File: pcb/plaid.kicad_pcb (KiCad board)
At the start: 2 copper layers, 228 x 98 mm, 127 parts, among them J2 AVR_ISP_6, SW1 SW_Push, SW10 SW_Push, SW11 SW_Push, SW12 SW_Push, SW13 SW_Push, SW14 SW_Push, SW15 SW_Push, SW16 SW_Push, SW17 SW_Push, SW18 SW_Push, SW19 SW_Push, SW2 SW_Push, SW20 SW_Push, SW21 SW_Push, SW22 SW_Push, SW23 SW_Push, SW24 SW_Push, SW25 SW_Push, SW26 SW_Push, SW27 SW_Push, SW28 SW_Push, SW29 SW_Push, SW3 SW_Push, SW30 SW_Push, SW31 SW_Push, SW32 SW_Push, SW33 SW_Push, SW34 SW_Push, SW35 SW_Push, SW36 SW_Push, SW37 SW_Push, SW38 SW_Push, SW39 SW_Push, SW4 SW_Push, SW40 SW_Push, SW41 SW_Push, SW42 SW_Push, SW43 SW_Push, SW44 SW_Push, SW45 SW_Push, SW46 SW_Push, SW47 SW_Push, SW48 SW_Push, SW49 SW_Push, SW5 SW_Push, SW50 RESET, SW51 BOOT, SW6 SW_Push, SW7 SW_Push, SW8 SW_Push, SW9 SW_Push, U1 ATMEGA328-PU, Y1 16MHz

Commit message: RGB LED setup
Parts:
- added 100n: 100n, Capacitor_THT:C_Disc_D4.3mm_W1.9mm_P5.00mm, F.Cu at (269.5, 59.3)
- added D49: SK6812, LED_SMD:LED_SK6812_PLCC4_5.0x5.0mm_P3.2mm, F.Cu at (259.5, 54.1)
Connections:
- net /i2c_SCL renamed Net-(U1-Pad28)
- U1 pad 27: /i2c_SDA -> /RGB_LED
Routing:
- net /RGB_LED: track 0.00 -> 33.5 mm, vias 0 -> 1
- net +5V: track 91.2 -> 123.2 mm
- net /i2c_SDA: track 2.69 -> 0.00 mm

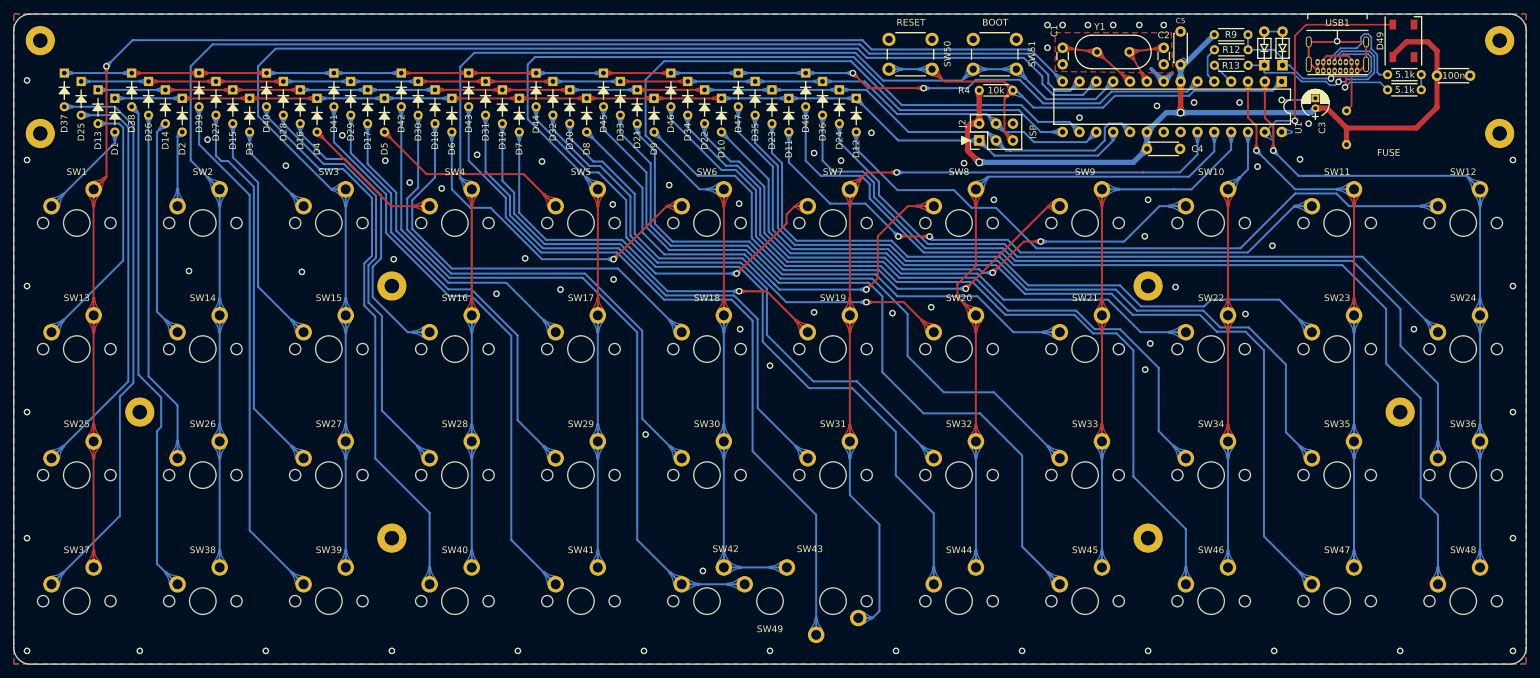
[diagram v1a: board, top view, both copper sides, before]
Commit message: Add usb-c, rgb led
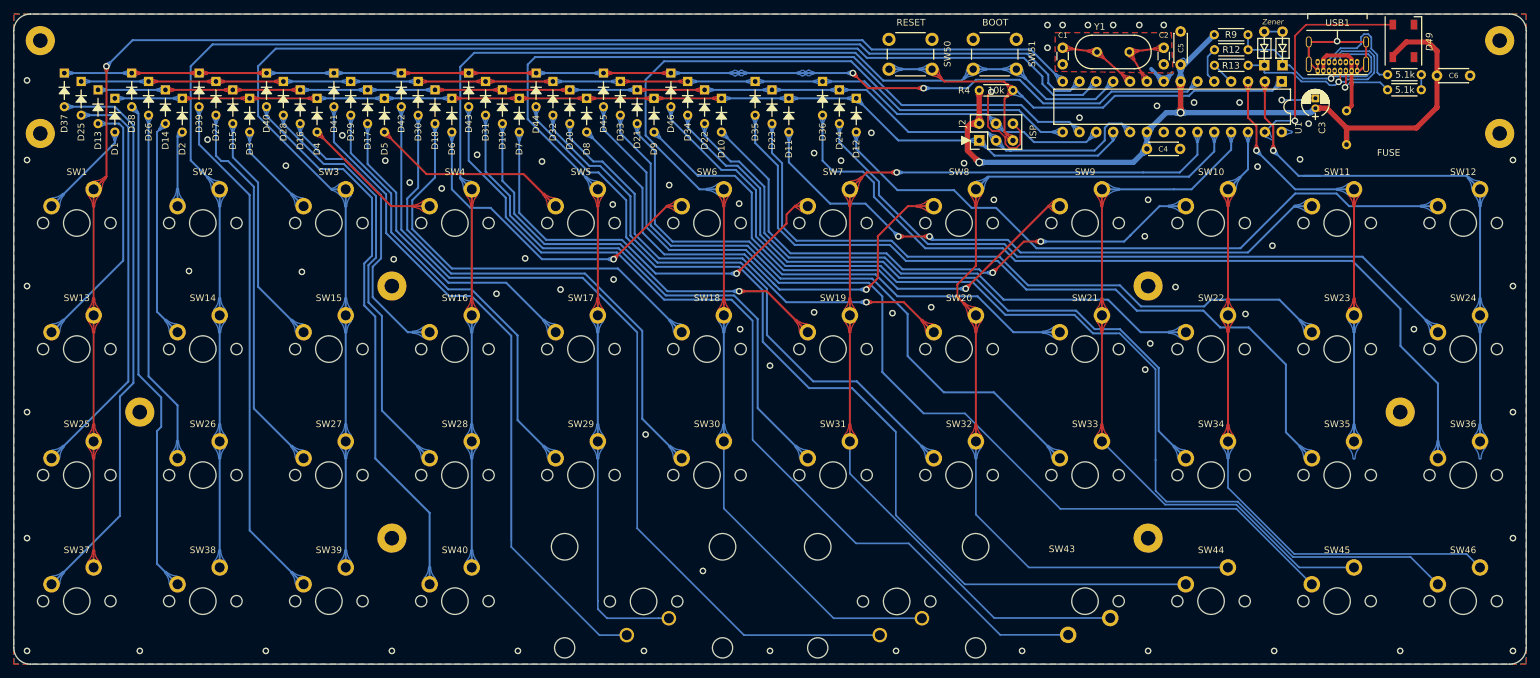
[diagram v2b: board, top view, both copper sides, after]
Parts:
- removed D47, D48: 1N4148, dm9_rc:D_DO-35_SOD27_P5.08mm_Horizontal
- removed SW47, SW48: SW_Push, SMKJP:SW_Cherry_MX1A_1.00u_PCB
- removed SW49: SW_Push, SMKJP:SW_Cherry_MX1A_2.0U_PCB_universal_center
- SW41, SW42: footprint SMKJP:SW_Cherry_MX1A_1.00u_PCB -> cftkb:SW_Cherry_MX1A_2.00u_PCBNOSCREEN
- moved SW43 38.0 mm to (211.5, 138.5)
- moved SW44 38.0 mm to (230.5, 138.5)
- moved SW45 38.0 mm to (249.5, 138.5)
- moved SW46 38.0 mm to (268.5, 138.5)
- moved SW42 26.6 mm to (180.6, 143.6), turned to 180 degrees
- moved SW41 8.60 mm to (142.4, 143.6), turned to 180 degrees
- renumbered 100n to C6
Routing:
- net Net-(D48-Pad2): track 150.9 -> 0.00 mm
- net Net-(D47-Pad2): track 140.5 -> 0.00 mm
- net Net-(D44-Pad2): track 108.8 -> 143.6 mm
- net /COL7: track 100.6 -> 133.9 mm
- net Net-(D46-Pad2): track 128.7 -> 161.4 mm
- net /COL9: track 66.9 -> 97.8 mm
- net Net-(D45-Pad2): track 120.2 -> 150.1 mm
- net /COL8: track 81.6 -> 108.5 mm
- net Net-(D43-Pad2): track 114.0 -> 140.3 mm
- net Net-(D42-Pad2): track 110.8 -> 133.3 mm
- net /COL6: track 127.0 -> 149.1 mm
- net /COL11: track 103.9 -> 84.9 mm
- net /COL10: track 85.1 -> 66.1 mm
- net /COL5: track 158.5 -> 176.8 mm
- net /COL4: track 168.5 -> 186.1 mm
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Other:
- net class VCC added: clearance 0.2, trace_width 0.6, via_dia 1, via_drill 0.6
- board text added: "D1"
- board text added: "D10"
- board text added: "D11"
- board text added: "D12"
- board text added: "D13"
- board text added: "D14"
- board text added: "D15"
- board text added: "D16"
- board text added: "D17"
- board text added: "D18"
- board text added: "D19"
- board text added: "D2"
- board text added: "D20"
- board text added: "D21"
- board text added: "D22"
- board text added: "D23"
- board text added: "D24"
- board text added: "D25"
- board text added: "D26"
- board text added: "D27"
- board text added: "D28"
- board text added: "D29"
- board text added: "D3"
- board text added: "D30"
- board text added: "D31"
- board text added: "D32"
- board text added: "D33"
- board text added: "D34"
- board text added: "D35"
- board text added: "D36"
- board text added: "D37"
- board text added: "D38"
- board text added: "D39"
- board text added: "D4"
- board text added: "D40"
- board text added: "D41"
- board text added: "D42"
- board text added: "D43"
- board text added: "D44"
- board text added: "D45"
- board text added: "D46"
- board text added: "D5"
- board text added: "D6"
- board text added: "D7"
- board text added: "D8"
- board text added: "D9"
- board text added: "Zener"
